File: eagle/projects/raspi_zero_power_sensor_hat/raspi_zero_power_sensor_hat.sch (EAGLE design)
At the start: 40 parts, among them J1 JST-PH-2TH-RA, J2 USB_MICROB_RECPT, Q1 PMOS-ENHANCE-8A, U1 BUFFER-1-SCHMITT, U2 TPS61089RNRR, U3 INA219AIDCNR, U4 MCP73831T

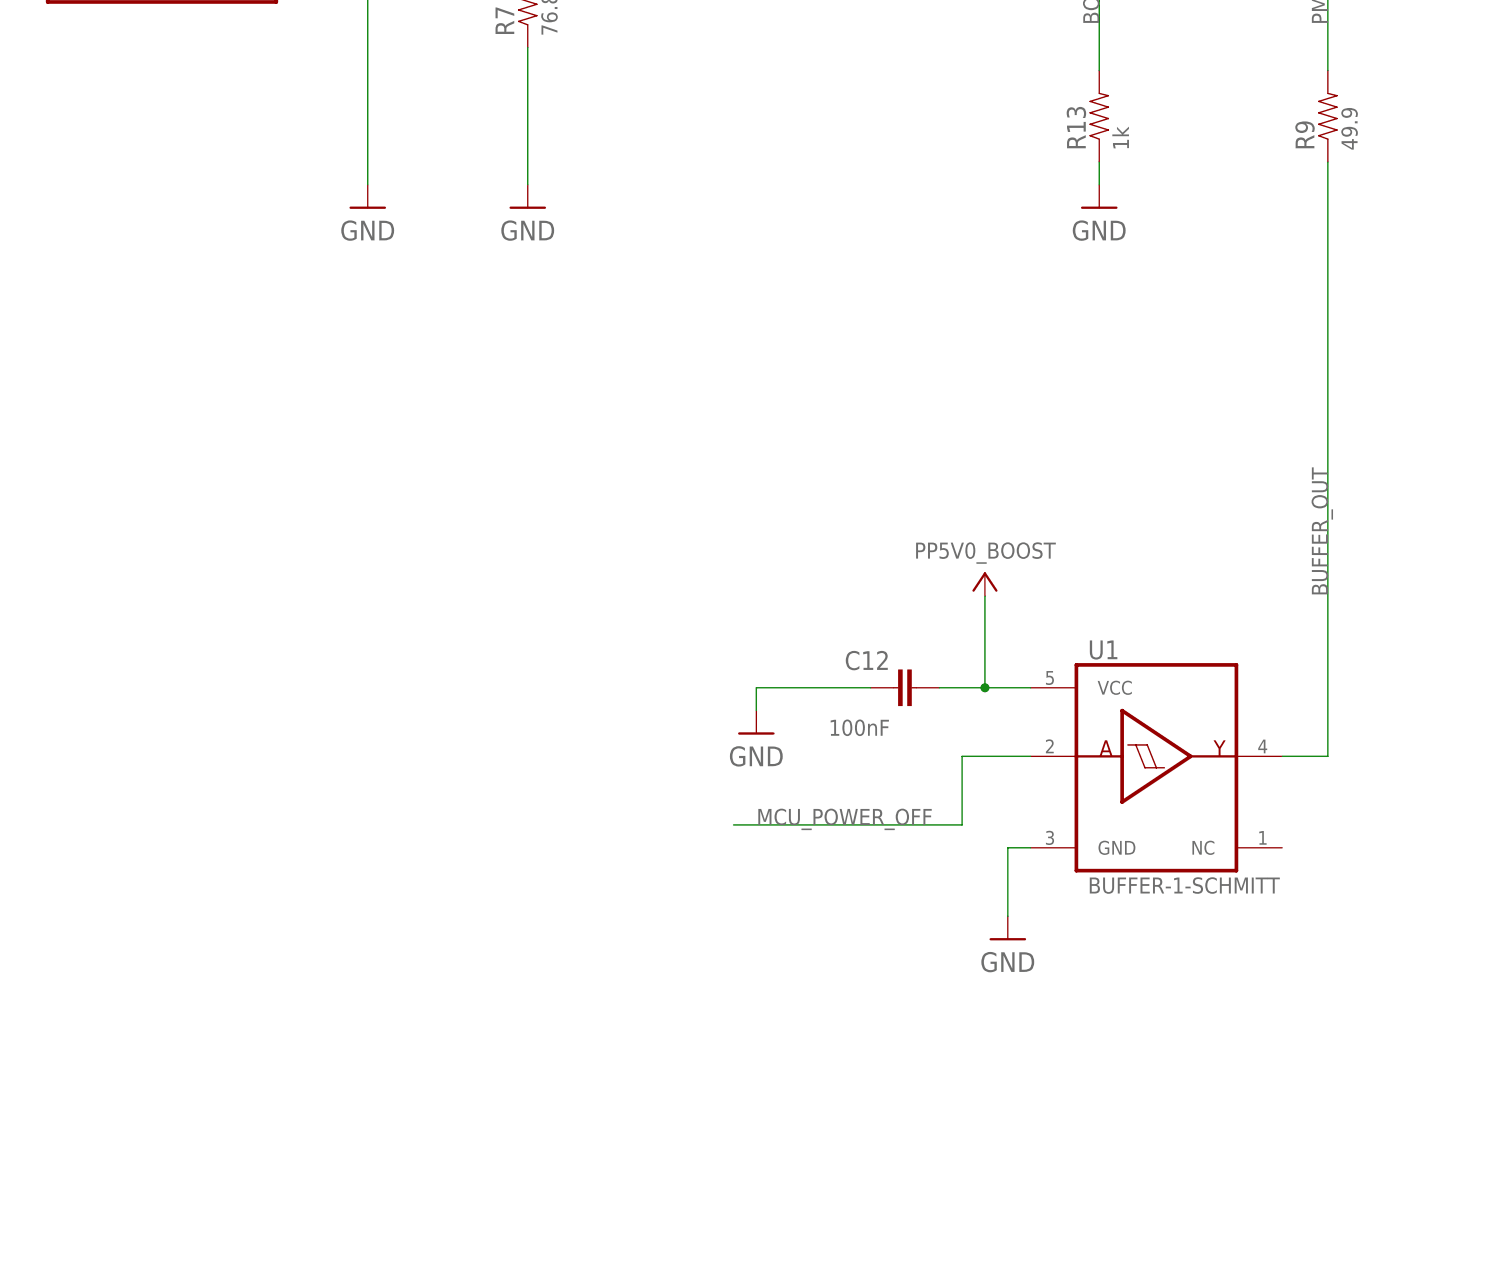
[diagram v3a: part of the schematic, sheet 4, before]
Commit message: added switch power off, and buffer input pull-down
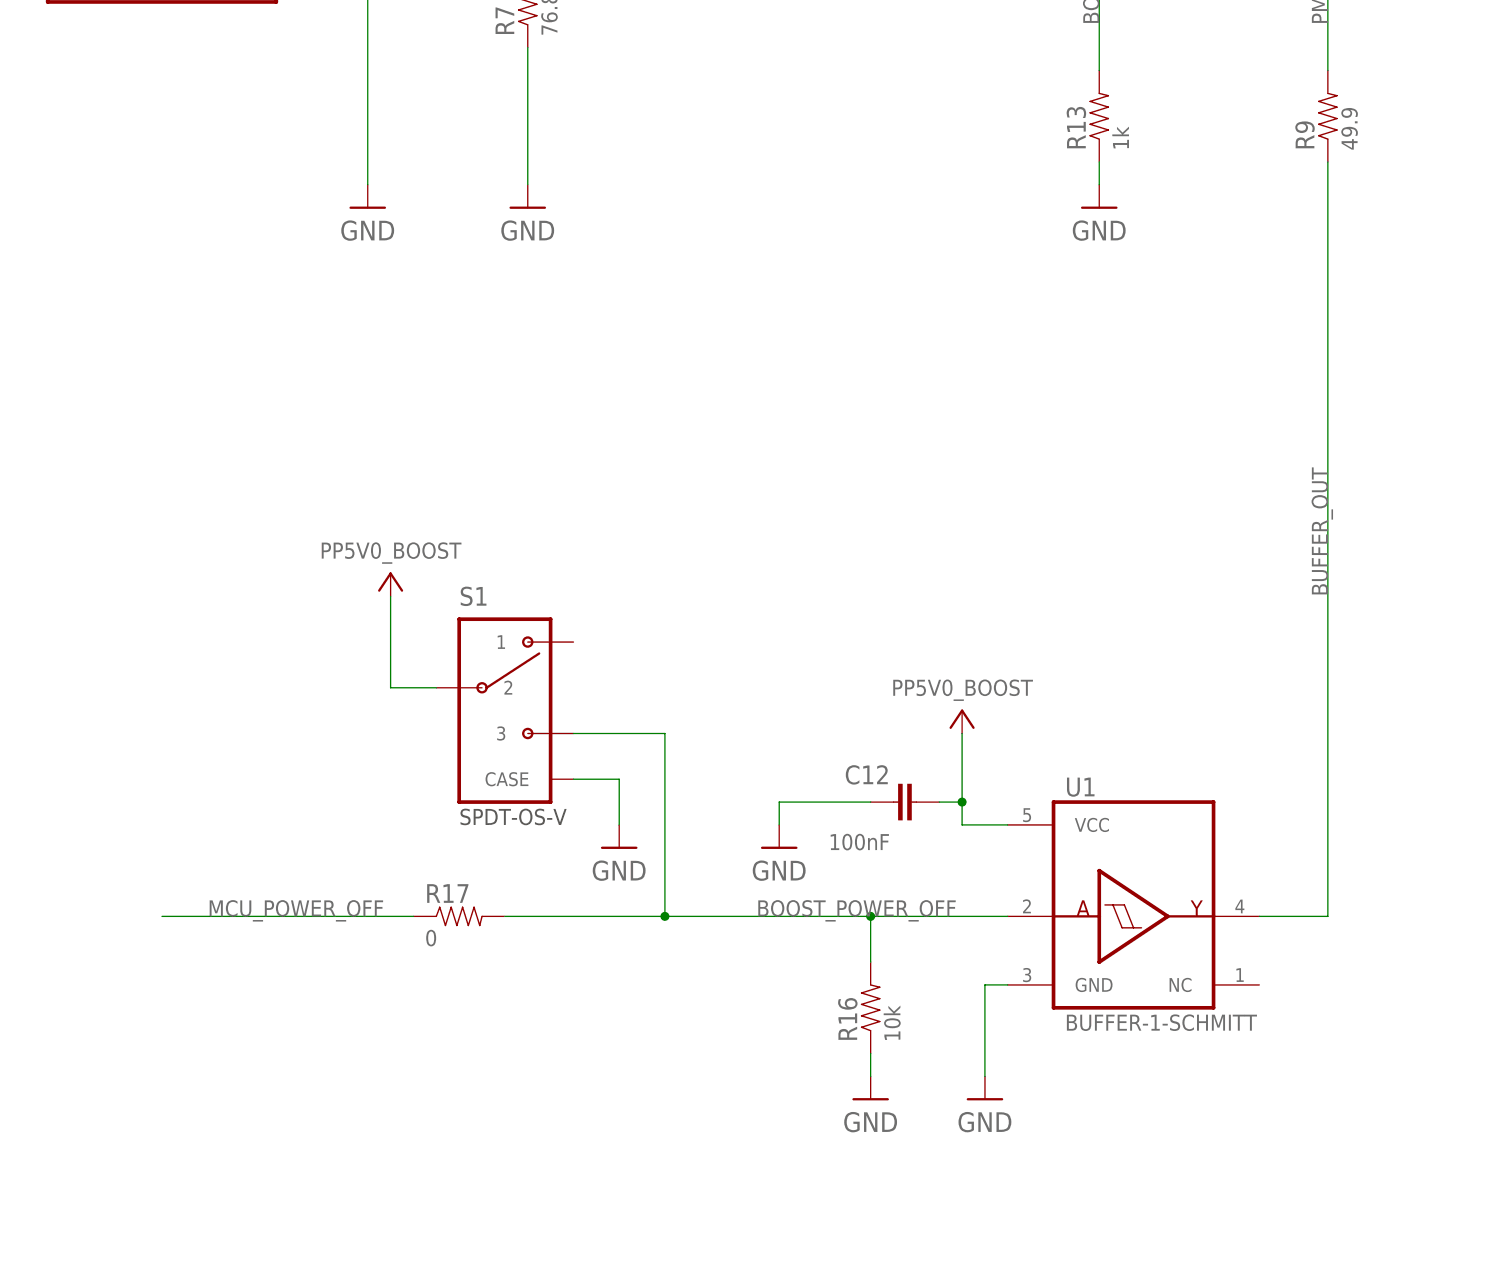
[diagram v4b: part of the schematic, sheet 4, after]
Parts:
- added R16: 10k, daqcs:RES_10R0_0603
- added R17: 0, daqcs:RES_0R0_0603
- added S1: SPDT-OS-V, daqcs:SPDT-CASE_SPDT-V_V
- added U5: MS560702BA03-50, daqcs:MS5607-02BA03_8SMD
- added U6: PCT2075D,118, daqcs:PCT2075D,118SOIC8
- added U7: SSCMNNN015PA2A3, daqcs:SSCMNNN015PA2A3_8SMD
- added U8: MAX11613EUA+, daqcs:MAX11613EUA+
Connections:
- new net BOOST_POWER_OFF: R16.2, R17.2, S1.3, U1.A
- net GND: now also R16.1, S1.CASE
- net MCU_POWER_OFF: now also R17.1; no longer U1.A
- net PP5V0_BOOST: now also S1.2
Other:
- moved on the sheet: C12, U1
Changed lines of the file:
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@@
 <part name="C13" library="daqcs" deviceset="CAP" device="_0603" technology="_10UF0" value="10uF"/>
 <part name="GND17" library="daqcs" deviceset="GND" device=""/>
+<part name="U5" library="daqcs" deviceset="MS5607" device="_8SMD" technology="-02BA03" value="MS560702BA03-50"/>
+<part name="U6" library="daqcs" deviceset="PCT2075" device="SOIC8" technology="D,118" value="PCT2075D,118"/>
+<part name="U7" library="daqcs" deviceset="SSCMNNN015PA" device="_8SMD" technology="2A3" value="SSCMNNN015PA2A3"/>
+<part name="R16" library="daqcs" deviceset="RES" device="_0603" technology="_10R0" value="10k"/>
+<part name="GND19" library="daqcs" deviceset="GND" device=""/>
+<part name="S1" library="daqcs" deviceset="SPDT-CASE" device="_V" technology="_SPDT-V" value="SPDT-OS-V"/>
+<part name="PP5V0_BOOST3" library="daqcs" deviceset="PP5V0_BOOST" device=""/>
+<part name="GND20" library="daqcs" deviceset="GND" device=""/>
+<part name="R17" library="daqcs" deviceset="RES" device="_0603" technology="_0R0" value="0"/>
+<part name="U8" library="daqcs" deviceset="MAX11613" device="" technology="EUA+" value="MAX11613EUA+"/>
 </parts>
 <sheets>
@@
 </sheet>
 <sheet>
-<description>MOUNT_TP_ADDR</description>
+<description>MOUNT_TP_CONN_ADDR</description>
 <plain>
 </plain>
@@
 <instance part="Q1" gate="G$1" x="353.06" y="190.5" rot="R90"/>
 <instance part="R9" gate="G$1" x="350.52" y="144.78" rot="R90"/>
-<instance part="U1" gate="G$1" x="330.2" y="73.66"/>
-<instance part="C12" gate="G$1" x="304.8" y="81.28" smashed="yes" rot="R90">
-<attribute name="NAME" x="301.879" y="85.344" size="2.0828" layer="95" ratio="10" rot="R180"/>
-<attribute name="VALUE" x="301.879" y="77.724" size="1.778" layer="96" ratio="10" rot="R180"/>
+<instance part="U1" gate="G$1" x="327.66" y="58.42"/>
+<instance part="C12" gate="G$1" x="304.8" y="68.58" smashed="yes" rot="R90">
+<attribute name="NAME" x="301.879" y="72.644" size="2.0828" layer="95" ratio="10" rot="R180"/>
+<attribute name="VALUE" x="301.879" y="65.024" size="1.778" layer="96" ratio="10" rot="R180"/>
 </instance>
-<instance part="GND11" gate="1" x="287.02" y="76.2"/>
-<instance part="GND12" gate="1" x="314.96" y="53.34"/>
+<instance part="GND11" gate="1" x="289.56" y="63.5"/>
+<instance part="GND12" gate="1" x="312.42" y="35.56"/>
 <instance part="PP5V0_BOOST1" gate="G$1" x="322.58" y="218.44"/>
-<instance part="PP5V0_BOOST2" gate="G$1" x="312.42" y="93.98"/>
+<instance part="PP5V0_BOOST2" gate="G$1" x="309.88" y="78.74"/>
 <instance part="PP5V0_BOOST_SW1" gate="G$1" x="383.54" y="218.44"/>
 <instance part="U4" gate="A" x="152.4" y="66.04"/>
@@
 <instance part="C13" gate="G$1" x="58.42" y="66.04"/>
 <instance part="GND17" gate="1" x="58.42" y="58.42"/>
+<instance part="R16" gate="G$1" x="299.72" y="45.72" rot="R90"/>
+<instance part="GND19" gate="1" x="299.72" y="35.56"/>
+<instance part="S1" gate="G$1" x="259.08" y="78.74"/>
+<instance part="PP5V0_BOOST3" gate="G$1" x="246.38" y="93.98"/>
+<instance part="GND20" gate="1" x="271.78" y="63.5"/>
+<instance part="R17" gate="G$1" x="254" y="55.88"/>
 </instances>
 <busses>
@@
 <pinref part="GND11" gate="1" pin="GND"/>
 <pinref part="C12" gate="G$1" pin="1"/>
-<wire x1="287.02" y1="78.74" x2="287.02" y2="81.28" width="0.1524" layer="91"/>
-<wire x1="287.02" y1="81.28" x2="299.72" y2="81.28" width="0.1524" layer="91"/>
+<wire x1="289.56" y1="66.04" x2="289.56" y2="68.58" width="0.1524" layer="91"/>
+<wire x1="289.56" y1="68.58" x2="299.72" y2="68.58" width="0.1524" layer="91"/>
 </segment>
 <segment>
 <pinref part="GND12" gate="1" pin="GND"/>
 <pinref part="U1" gate="G$1" pin="GND"/>
-<wire x1="314.96" y1="55.88" x2="314.96" y2="63.5" width="0.1524" layer="91"/>
-<wire x1="314.96" y1="63.5" x2="317.5" y2="63.5" width="0.1524" layer="91"/>
+<wire x1="312.42" y1="38.1" x2="312.42" y2="48.26" width="0.1524" layer="91"/>
+<wire x1="312.42" y1="48.26" x2="314.96" y2="48.26" width="0.1524" layer="91"/>
 </segment>
 <segment>
@@
 <pinref part="GND17" gate="1" pin="GND"/>
 <wire x1="58.42" y1="63.5" x2="58.42" y2="60.96" width="0.1524" layer="91"/>
+</segment>
+<segment>
+<pinref part="R16" gate="G$1" pin="1"/>
+<pinref part="GND19" gate="1" pin="GND"/>
+<wire x1="299.72" y1="40.64" x2="299.72" y2="38.1" width="0.1524" layer="91"/>
+</segment>
+<segment>
+<pinref part="S1" gate="G$1" pin="CASE"/>
+<wire x1="266.7" y1="71.12" x2="271.78" y2="71.12" width="0.1524" layer="91"/>
+<pinref part="GND20" gate="1" pin="GND"/>
+<wire x1="271.78" y1="71.12" x2="271.78" y2="66.04" width="0.1524" layer="91"/>
 </segment>
 </net>
@@
 </segment>
 </net>
-<net name="MCU_POWER_OFF" class="0">
+<net name="BOOST_POWER_OFF" class="0">
 <segment>
 <pinref part="U1" gate="G$1" pin="A"/>
-<wire x1="317.5" y1="73.66" x2="309.88" y2="73.66" width="0.1524" layer="91"/>
-<wire x1="309.88" y1="73.66" x2="309.88" y2="66.04" width="0.1524" layer="91"/>
-<wire x1="309.88" y1="66.04" x2="284.48" y2="66.04" width="0.1524" layer="91"/>
-<label x="287.02" y="66.04" size="1.778" layer="95"/>
+<wire x1="314.96" y1="55.88" x2="299.72" y2="55.88" width="0.1524" layer="91"/>
+<label x="287.02" y="55.88" size="1.778" layer="95"/>
+<pinref part="R16" gate="G$1" pin="2"/>
+<wire x1="299.72" y1="55.88" x2="276.86" y2="55.88" width="0.1524" layer="91"/>
+<wire x1="299.72" y1="50.8" x2="299.72" y2="55.88" width="0.1524" layer="91"/>
+<junction x="299.72" y="55.88"/>
+<pinref part="S1" gate="G$1" pin="3"/>
+<wire x1="266.7" y1="76.2" x2="276.86" y2="76.2" width="0.1524" layer="91"/>
+<wire x1="276.86" y1="76.2" x2="276.86" y2="55.88" width="0.1524" layer="91"/>
+<pinref part="R17" gate="G$1" pin="2"/>
+<wire x1="276.86" y1="55.88" x2="259.08" y2="55.88" width="0.1524" layer="91"/>
+<junction x="276.86" y="55.88"/>
 </segment>
 </net>
@@
 <label x="350.52" y="91.44" size="1.778" layer="95" rot="R90"/>
 <pinref part="U1" gate="G$1" pin="Y"/>
-<wire x1="350.52" y1="139.7" x2="350.52" y2="73.66" width="0.1524" layer="91"/>
-<wire x1="350.52" y1="73.66" x2="345.44" y2="73.66" width="0.1524" layer="91"/>
+<wire x1="350.52" y1="139.7" x2="350.52" y2="55.88" width="0.1524" layer="91"/>
+<wire x1="350.52" y1="55.88" x2="342.9" y2="55.88" width="0.1524" layer="91"/>
 </segment>
 </net>
@@
 </segment>
 <segment>
-<wire x1="312.42" y1="91.44" x2="312.42" y2="81.28" width="0.1524" layer="91"/>
+<wire x1="309.88" y1="76.2" x2="309.88" y2="68.58" width="0.1524" layer="91"/>
 <pinref part="U1" gate="G$1" pin="VCC"/>
-<wire x1="312.42" y1="81.28" x2="317.5" y2="81.28" width="0.1524" layer="91"/>
+<wire x1="309.88" y1="68.58" x2="309.88" y2="66.04" width="0.1524" layer="91"/>
+<wire x1="309.88" y1="66.04" x2="314.96" y2="66.04" width="0.1524" layer="91"/>
+<pinref part="PP5V0_BOOST2" gate="G$1" pin="PP5V0_BOOST"/>
 <pinref part="C12" gate="G$1" pin="2"/>
-<wire x1="307.34" y1="81.28" x2="312.42" y2="81.28" width="0.1524" layer="91"/>
-<junction x="312.42" y="81.28"/>
-<pinref part="PP5V0_BOOST2" gate="G$1" pin="PP5V0_BOOST"/>
+<wire x1="309.88" y1="68.58" x2="307.34" y2="68.58" width="0.1524" layer="91"/>
+<junction x="309.88" y="68.58"/>
+</segment>
+<segment>
+<wire x1="246.38" y1="91.44" x2="246.38" y2="81.28" width="0.1524" layer="91"/>
+<pinref part="S1" gate="G$1" pin="2"/>
+<wire x1="246.38" y1="81.28" x2="251.46" y2="81.28" width="0.1524" layer="91"/>
+<pinref part="PP5V0_BOOST3" gate="G$1" pin="PP5V0_BOOST"/>
 </segment>
 </net>
@@
 </segment>
 </net>
+<net name="MCU_POWER_OFF" class="0">
+<segment>
+<pinref part="R17" gate="G$1" pin="1"/>
+<wire x1="248.92" y1="55.88" x2="220.98" y2="55.88" width="0.1524" layer="91"/>
+<label x="226.06" y="55.88" size="1.778" layer="95"/>
+</segment>
+</net>
 </nets>
 </sheet>
@@
 <instance part="R5" gate="G$1" x="104.14" y="38.1" rot="R90"/>
 <instance part="GND5" gate="1" x="93.98" y="25.4"/>
+<instance part="U5" gate="G$1" x="129.54" y="215.9"/>
+<instance part="U6" gate="A" x="200.66" y="210.82"/>
+<instance part="U7" gate="G$1" x="193.04" y="157.48"/>
+<instance part="U8" gate="A" x="299.72" y="165.1"/>
 </instances>
 <busses>

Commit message: added all pi hat schematic elements
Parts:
- removed S1: SPDT-OS-V, daqcs:SPDT-CASE_SPDT-V_V
- added C14, C15, C16, C17: 100nF, daqcs:CAP_100NF0_0603
- added J3: HEADER-1x2-2.54MM, daqcs:HEADER-1X2-254MM_1X2_254MM_TH
- added J4: MOL-KK-2-V, daqcs:MOLKK_2PIN2V_2V
- added J5: RECEPTACLE-2x7-2.54MM, daqcs:RECEPTICAL-2X7-254MM-PIZERO_2X7_254MM_TH
- added J6: MOL-KK-4-RA, daqcs:MOLKK_4PIN_4RA_RA
- added R18, R19, R20, R21: 0, daqcs:RES_0R0_0603
- added R22: 10k, daqcs:RES_10R0_0603
- added R23, R24: 2k, daqcs:RES_2R0_0603
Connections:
- removed net BOOST_POWER_OFF: R16.2, R17.2, S1.3, U1.A
- new net ADC_AIN0: U8.AIN0
- new net ADC_AIN1: U8.AIN1
- new net ADC_AIN2: U8.AIN2
- new net ADC_AIN3/REF: U8.AIN3/REF
- new net BOOST_LOAD_DISABLE: R16.2, R17.2, U1.A
- new net MS_CSB: R18.2, U5.CSB@1, U5.CSB@2
- new net TEMP_A0: R19.2, U6.A0
- new net TEMP_A1: R20.2, U6.A1
- new net TEMP_A2: R21.2, U6.A2
- new net TEMP_ALERT: J5.GPIO4/GPIO_GCLK, R22.1, U6.OS
- new net UART_RASPI_RXD_MCU_TXD: J5.GPIO15/RXD0, J6.4
- new net UART_RASPI_TXD_MCU_RXD: J5.GPIO14/TXD0, J6.2
- new net VBAT_J: J3.2, R1.2A
- net GND: now also C14.1, C15.2, C16.1, C17.1, J4.2, J5.GND@1, J5.GND@2, J5.GND@3, J6.3, R18.1, R19.1, R20.1, R21.1, U5.GND, U6.GND, U7.GND, U8.GND; no longer S1.CASE
- net I2C1_RASPI_SCL: now also J5.GPIO3/SCL1, R23.1, U5.SCLK, U6.SCL, U7.SCL, U8.SCL
- net I2C1_RASPI_SDA: now also J5.GPIO2/SDA1, R24.1, U5.SDI/SDA, U6.SDA, U7.SDA, U8.SDA
- net MCU_POWER_OFF: now also J6.1
- net PP3V3_RASPI: now also C14.2, C15.1, C16.2, C17.2, J5.3V3, R22.2, R23.2, R24.2, U5.PS, U5.VDD, U6.VCC, U7.VCC, U8.VDD
- net PP5V0_BOOST: no longer S1.2
- net PP5V0_BOOST_SW: now also J5.5V0@1, J5.5V0@2
- net PP5V0_USB: now also J4.1
- net VBAT: now also J3.1; no longer R1.2A
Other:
- note added: "(Honeywell)"
- note added: "(TE)"
- note added: "12-bit ADC"
- note added: "5.3V Power"
- note added: "5V Power"
- note added: "Current/Voltage"
- note added: "HOST MCU CONNECTOR"
- note added: "HOST/RASPI CONNECTORS and SENSORS"
- note added: "Pressure Sensor"
- note added: "RASPBERRY PI HEADER"
- note added: "Sense Amplifier"
- note added: "Temperature Sensor"
- note added: "from Raspi"
- note added: "to Raspi"
- moved on the sheet: C13, C2, J1, R1, R15, R17, R4, R5, U3, U5, U6, U7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

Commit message: all electrical connections set for PI sensor HAT. Still need to add block diagram, mounting holes/TPs and, and I2C ADDR Table
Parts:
- added C18, C19: 100nF, daqcs:CAP_100NF0_0603
- added J7: MOL-KK-3P-V, daqcs:MOLKK_3PIN_3V_V
- added Q2: PMOS-ENHANCE-8A, daqcs:PMOS-1G-1S-4D_PMOS-6P_TSOP-6
- added R25: 4.7k, daqcs:RES_4R7_0603
- added R26: 0, daqcs:RES_0R0_0603
- added R27: 49.9, daqcs:RES_0R499_0603
- added R28, R29: 10k, daqcs:RES_10R0_0603
- added U9: BUFFER-1-SCHMITT, daqcs:BUFFER-1-SCHMITT_BUF1_TSSOP5
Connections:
- net BUFFER_OUT renamed MCU_BUFFER_OUT
- net TEMP_A0 renamed TEMP_I2C_A0
- net TEMP_A1 renamed TEMP_I2C_A1
- net TEMP_A2 renamed TEMP_I2C_A2
- removed net PMOS_GATE: Q1.G, R9.2
- removed net TEMP_ALERT: J5.GPIO4/GPIO_GCLK, R22.1, U6.OS
- new net RASPI_PMOS_GATE: Q1.G, R29.1, R9.2
- new net TEMP_1WIRE_BI: J5.GPIO4/GPIO_GCLK/1-WIRE, J7.3, R25.1
- new net TEMP_I2C_ALERT: J5.GPIO17/GPIO_GEN0, R22.1, U6.OS
- new net USB_BUFFER_OUT: R27.1, U9.Y
- new net VBAT_LOAD_DISABLE: R26.1, U9.A
- new net VBAT_PMOS_GATE: Q2.G, R27.2, R28.1
- net CHG_ON: now also R11.1; no longer R11.2
- net GND: now also C18.2, C19.1, J7.2, R28.2, R29.2, U9.GND
- net PP3V3_RASPI: now also C18.1, J7.1, R25.2
- net PP5V0_USB: now also C19.2, R11.2, R26.2, U9.VCC; no longer R11.1
- net VBAT: now also Q2.S
- net VBAT_J: now also Q2.D@1, Q2.D@2, Q2.D@3, Q2.D@4
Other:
- note added: "3xAA Battery: ~3.7V to 4.6V"
- note added: "5V Boost SMPS"
- note added: "Battery Current: ~400mA (AVG)"
- note added: "CHARGING LOAD"
- note added: "Charger Status LEDs"
- note added: "Complement of CSB"
- note added: "DISABLE"
- note added: "EXTERNAL TEMPERATURE"
- note added: "FROM MCU"
- note added: "I2C Addr: 0x28/0x29 (W/R)"
- note added: "I2C Addr: 0x68/0x69 (W/R)"
- note added: "I2C Addr: 0x80/0x81 (W/R)"
- note added: "I2C Addr: 0x90/0x91 (W/R)"
- note added: "I2C Addr: 0xEE/0xEF (W/R)"
- note added: "LEDS"
- note added: "LiPo Battery Charger"
- note added: "LiPo Battery: ~3.0V-4.2V"
- note added: "MOUNT_TP_CONFIG"
- note added: "PI_MCU_CONNECT_AND_SENSORS"
- note added: "POWER STATUS"
- note added: "POWER TO"
- note added: "POWER_ENTRY_BOOST_CHARGER"
- note added: "PROG PD sets charging"
- note added: "R8 sets switching"
- note added: "RASPI HARD RESET"
- note added: "SENSOR CONNECTOR"
- note added: "SYSTEM"
- note added: "System Current: ~250mA (AVG)"
- note added: "current limit = 500mA"
- note added: "frequency = ~500kHz"
- note added: "sets LSB of I2C ADDR"
- note added: "~500mA (PEAK)"
- note added: "~775mA (PEAK)"
- note removed: "MOUNT_TP_ADDR"
- moved on the sheet: C1, C10, C12, C13, C3, C4, C5, C6, C9, DS1, DS2, DS3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
